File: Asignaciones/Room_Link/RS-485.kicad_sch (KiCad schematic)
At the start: 0 parts

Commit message: ROOM-LINK update KICAD
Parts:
- added C5: 1 uF, Capacitor_SMD:C_0805_2012Metric_Pad1.18x1.45mm_HandSolder, symbol Device:C
- added C6: 0.1 uF, Capacitor_SMD:C_0805_2012Metric_Pad1.18x1.45mm_HandSolder, symbol Device:C
- added D14: SMBJ12CA, nuevo simbolo:SMBJ12CA, symbol SMBJ12CA:SMBJ12CA
- added D15: SM712-02HTG, sm712:SM71202HTG, symbol SM712-02HTG:SM712-02HTG
- added R27, R29: 10, Resistor_SMD:R_0805_2012Metric_Pad1.20x1.40mm_HandSolder, symbol Device:R
- added R28: 10 1%, Resistor_SMD:R_0805_2012Metric_Pad1.20x1.40mm_HandSolder, symbol Device:R
- added U3: SP485ECN-L, footprints:NSOIC-8-L, symbol 2023-07-02_02-34-59:SP485ECN-L
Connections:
- net COM_RS485_LCD: now also R28.1
- net CON-LCDA: now also R29.2
- net CON-LCDB+: now also R27.2
- net Rx_RS485_lcd: now also U3.4 (DI)
- net Tx_RS485_LCD: now also U3.1 (RO)
- new net: D14.2, D15.1, R29.1, U3.6 (A)
- new net: D14.1, D15.2, R27.1, U3.7 (B)
- new net: R28.2, U3.2 (*RE), U3.3 (DE)
- new net +5V: C5.1, C6.1, U3.8 (VCC)
- new net GND: C5.2, C6.2, D15.3, U3.5 (GND)

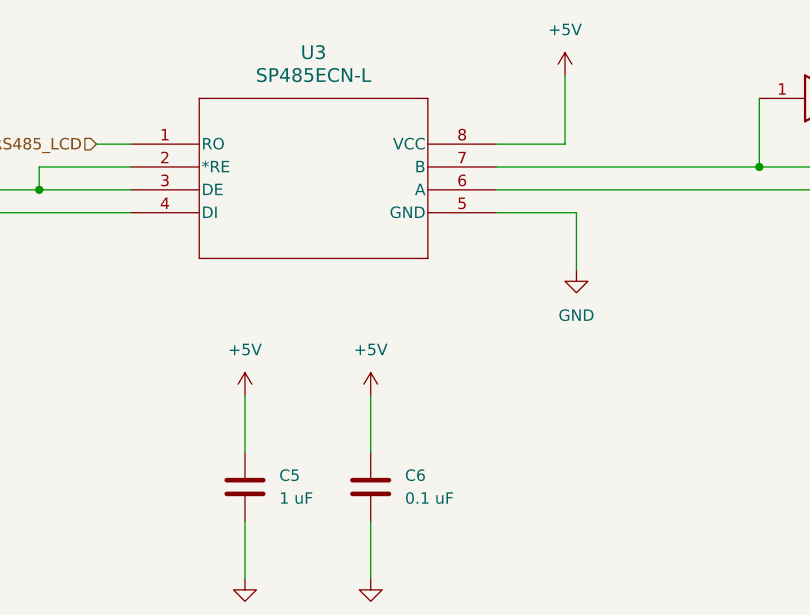
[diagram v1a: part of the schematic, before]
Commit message: Place component Added & routing
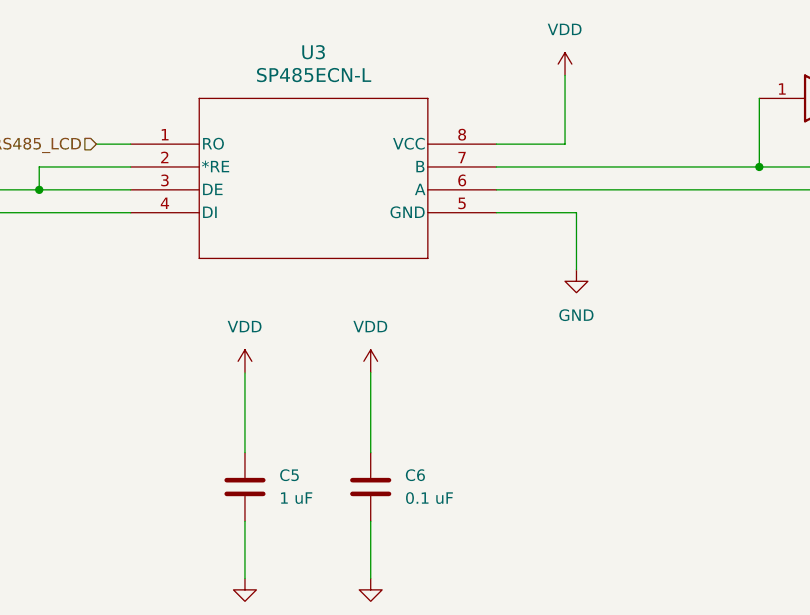
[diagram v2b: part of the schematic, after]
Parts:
- C5, C6: footprint Capacitor_SMD:C_0805_2012Metric_Pad1.18x1.45mm_HandSolder -> Capacitor_SMD:C_0805_2012Metric
- D15: footprint sm712:SM71202HTG -> Package_TO_SOT_SMD:SOT-23
- R27, R28, R29: footprint Resistor_SMD:R_0805_2012Metric_Pad1.20x1.40mm_HandSolder -> Resistor_SMD:R_0805_2012Metric
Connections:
- net +5V renamed VDD
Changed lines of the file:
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@@
+    (stroke (width 0) (type default))
+  )
+  (wire (pts (xy 138.43 119.38) (xy 138.43 128.27))
     (stroke (width 0) (type default))
   )
@@
     (stroke (width 0) (type default))
   )
+  (wire (pts (xy 124.46 119.38) (xy 124.46 128.27))
+    (stroke (width 0) (type default))
+  )
   (wire (pts (xy 193.04 96.52) (xy 213.36 96.52))
     (stroke (width 0) (type default))
   )
-  (wire (pts (xy 124.46 121.92) (xy 124.46 128.27))
-    (stroke (width 0) (type default))
-  )
   (wire (pts (xy 124.46 135.89) (xy 124.46 142.24))
     (stroke (width 0) (type default))
@@
   )
   (wire (pts (xy 101.6 99.06) (xy 111.76 99.06))
-    (stroke (width 0) (type default))
-  )
-  (wire (pts (xy 138.43 121.92) (xy 138.43 128.27))
     (stroke (width 0) (type default))
   )
@@
   (hierarchical_label "CON-LCDA" (shape input) (at 236.22 99.06 0) (fields_autoplaced)
     (effects (font (size 1.27 1.27)) (justify left))
-  )
-  (symbol (lib_id "power:+5V") (at 124.46 121.92 0) (unit 1)
-    (in_bom yes) (on_board yes) (dnp no) (fields_autoplaced)
-    (property "Reference" "#PWR034" (at 124.46 125.73 0)
-      (effects (font (size 1.27 1.27)) hide)
-    )
-    (property "Value" "+5V" (at 124.46 116.84 0)
-      (effects (font (size 1.27 1.27)))
-    )
-    (property "Footprint" "" (at 124.46 121.92 0)
-      (effects (font (size 1.27 1.27)) hide)
-    )
-    (property "Datasheet" "" (at 124.46 121.92 0)
-      (effects (font (size 1.27 1.27)) hide)
-    )
-    (pin "1")
-    (instances
-      (project "Room_Link"
-        (path "/c4ebd78f-0c54-42fb-8411-155772684713/6ffab1c0-a902-4896-acce-96f8f8ea2f51/8d7c8ed9-ca53-4563-8d3f-2b2a3ea9afb6"
-          (reference "#PWR034") (unit 1)
-        )
-      )
-    )
   )
   (symbol (lib_id "Device:R") (at 217.17 99.06 90) (unit 1)
@@
       (effects (font (size 1.27 1.27)) (justify left))
     )
-    (property "Footprint" "Resistor_SMD:R_0805_2012Metric_Pad1.20x1.40mm_HandSolder" (at 217.17 100.838 90)
+    (property "Footprint" "Resistor_SMD:R_0805_2012Metric" (at 217.17 100.838 90)
       (effects (font (size 1.27 1.27)) hide)
     )
@@
       (effects (font (size 1.27 1.27)) (justify left))
     )
-    (property "Footprint" "Capacitor_SMD:C_0805_2012Metric_Pad1.18x1.45mm_HandSolder" (at 125.4252 135.89 0)
+    (property "Footprint" "Capacitor_SMD:C_0805_2012Metric" (at 125.4252 135.89 0)
       (effects (font (size 1.27 1.27)) hide)
     )
@@
       (effects (font (size 1.27 1.27)) (justify left))
     )
-    (property "Footprint" "Capacitor_SMD:C_0805_2012Metric_Pad1.18x1.45mm_HandSolder" (at 139.3952 135.89 0)
+    (property "Footprint" "Capacitor_SMD:C_0805_2012Metric" (at 139.3952 135.89 0)
       (effects (font (size 1.27 1.27)) hide)
     )
@@
         (path "/c4ebd78f-0c54-42fb-8411-155772684713/6ffab1c0-a902-4896-acce-96f8f8ea2f51/8d7c8ed9-ca53-4563-8d3f-2b2a3ea9afb6"
           (reference "C6") (unit 1)
+        )
+      )
+    )
+  )
+  (symbol (lib_id "power:VDD") (at 124.46 119.38 0) (unit 1)
+    (in_bom yes) (on_board yes) (dnp no) (fields_autoplaced)
+    (property "Reference" "#PWR077" (at 124.46 123.19 0)
+      (effects (font (size 1.27 1.27)) hide)
+    )
+    (property "Value" "VDD" (at 124.46 114.3 0)
+      (effects (font (size 1.27 1.27)))
+    )
+    (property "Footprint" "" (at 124.46 119.38 0)
+      (effects (font (size 1.27 1.27)) hide)
+    )
+    (property "Datasheet" "" (at 124.46 119.38 0)
+      (effects (font (size 1.27 1.27)) hide)
+    )
+    (pin "1")
+    (instances
+      (project "Room_Link"
+        (path "/c4ebd78f-0c54-42fb-8411-155772684713/6ffab1c0-a902-4896-acce-96f8f8ea2f51/8d7c8ed9-ca53-4563-8d3f-2b2a3ea9afb6"
+          (reference "#PWR077") (unit 1)
         )
       )
@@
       (effects (font (size 1.27 1.27)))
     )
-    (property "Footprint" "Resistor_SMD:R_0805_2012Metric_Pad1.20x1.40mm_HandSolder" (at 88.9 100.838 90)
+    (property "Footprint" "Resistor_SMD:R_0805_2012Metric" (at 88.9 100.838 90)
       (effects (font (size 1.27 1.27)) hide)
     )
@@
     )
   )
-  (symbol (lib_id "power:+5V") (at 138.43 121.92 0) (unit 1)
-    (in_bom yes) (on_board yes) (dnp no) (fields_autoplaced)
-    (property "Reference" "#PWR035" (at 138.43 125.73 0)
-      (effects (font (size 1.27 1.27)) hide)
-    )
-    (property "Value" "+5V" (at 138.43 116.84 0)
-      (effects (font (size 1.27 1.27)))
-    )
-    (property "Footprint" "" (at 138.43 121.92 0)
-      (effects (font (size 1.27 1.27)) hide)
-    )
-    (property "Datasheet" "" (at 138.43 121.92 0)
-      (effects (font (size 1.27 1.27)) hide)
-    )
-    (pin "1")
-    (instances
-      (project "Room_Link"
-        (path "/c4ebd78f-0c54-42fb-8411-155772684713/6ffab1c0-a902-4896-acce-96f8f8ea2f51/8d7c8ed9-ca53-4563-8d3f-2b2a3ea9afb6"
-          (reference "#PWR035") (unit 1)
+  (symbol (lib_id "power:VDD") (at 138.43 119.38 0) (unit 1)
+    (in_bom yes) (on_board yes) (dnp no) (fields_autoplaced)
+    (property "Reference" "#PWR034" (at 138.43 123.19 0)
+      (effects (font (size 1.27 1.27)) hide)
+    )
+    (property "Value" "VDD" (at 138.43 114.3 0)
+      (effects (font (size 1.27 1.27)))
+    )
+    (property "Footprint" "" (at 138.43 119.38 0)
+      (effects (font (size 1.27 1.27)) hide)
+    )
+    (property "Datasheet" "" (at 138.43 119.38 0)
+      (effects (font (size 1.27 1.27)) hide)
+    )
+    (pin "1")
+    (instances
+      (project "Room_Link"
+        (path "/c4ebd78f-0c54-42fb-8411-155772684713/6ffab1c0-a902-4896-acce-96f8f8ea2f51/8d7c8ed9-ca53-4563-8d3f-2b2a3ea9afb6"
+          (reference "#PWR034") (unit 1)
         )
       )
@@
       (effects (font (size 1.27 1.27)) (justify right))
     )
-    (property "Footprint" "sm712:SM71202HTG" (at 285.42 120.65 0)
+    (property "Footprint" "Package_TO_SOT_SMD:SOT-23" (at 285.42 120.65 0)
       (effects (font (size 1.27 1.27)) (justify left top) hide)
     )
@@
     )
   )
-  (symbol (lib_id "power:+5V") (at 160.02 86.36 0) (unit 1)
-    (in_bom yes) (on_board yes) (dnp no) (fields_autoplaced)
-    (property "Reference" "#PWR038" (at 160.02 90.17 0)
-      (effects (font (size 1.27 1.27)) hide)
-    )
-    (property "Value" "+5V" (at 160.02 81.28 0)
+  (symbol (lib_id "power:VDD") (at 160.02 86.36 0) (unit 1)
+    (in_bom yes) (on_board yes) (dnp no) (fields_autoplaced)
+    (property "Reference" "#PWR035" (at 160.02 90.17 0)
+      (effects (font (size 1.27 1.27)) hide)
+    )
+    (property "Value" "VDD" (at 160.02 81.28 0)
       (effects (font (size 1.27 1.27)))
     )
@@
       (project "Room_Link"
         (path "/c4ebd78f-0c54-42fb-8411-155772684713/6ffab1c0-a902-4896-acce-96f8f8ea2f51/8d7c8ed9-ca53-4563-8d3f-2b2a3ea9afb6"
-          (reference "#PWR038") (unit 1)
+          (reference "#PWR035") (unit 1)
         )
       )
@@
       (effects (font (size 1.27 1.27)) (justify left))
     )
-    (property "Footprint" "Resistor_SMD:R_0805_2012Metric_Pad1.20x1.40mm_HandSolder" (at 217.17 98.298 90)
-      (effects (font (size 1.27 1.27)) hide)
-    )
+    (property "Footprint" "Resistor_SMD:R_0805_2012Metric" (at 217.17 98.298 90)
+      (effects (font (size 1.27 1.27)) hide)
+    )
